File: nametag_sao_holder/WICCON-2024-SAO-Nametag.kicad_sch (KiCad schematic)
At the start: 25 parts, among them J1 SAO, J2 SAO, J3 SAO, J4 SAO, J5 SAO, J6 SAO, J7 SAO, J8 SAO, SW1 ON/OFF, U1 QX2303L33E

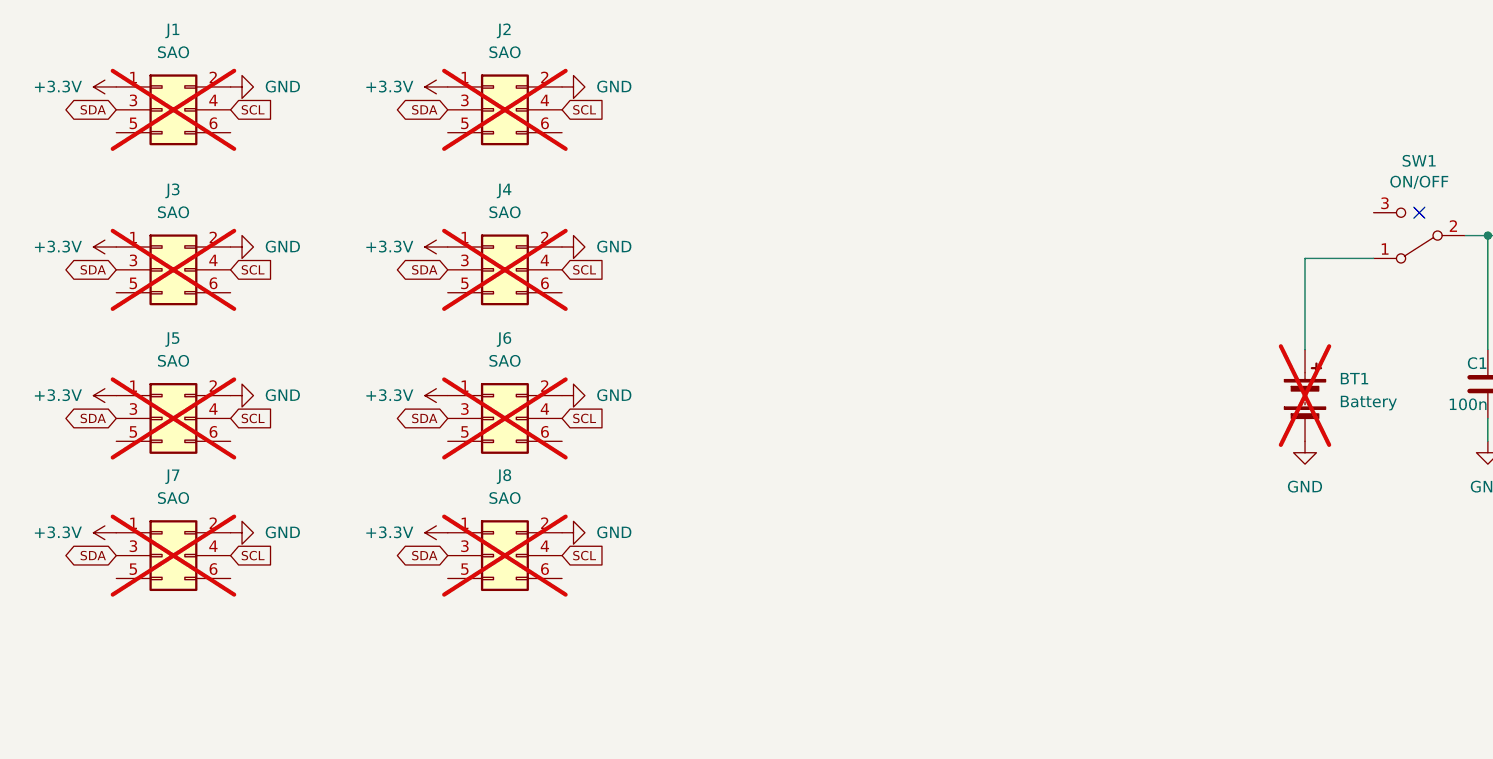
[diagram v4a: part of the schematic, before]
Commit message: Add SAO connector LCSC number, place all SAO connectors & battery holder
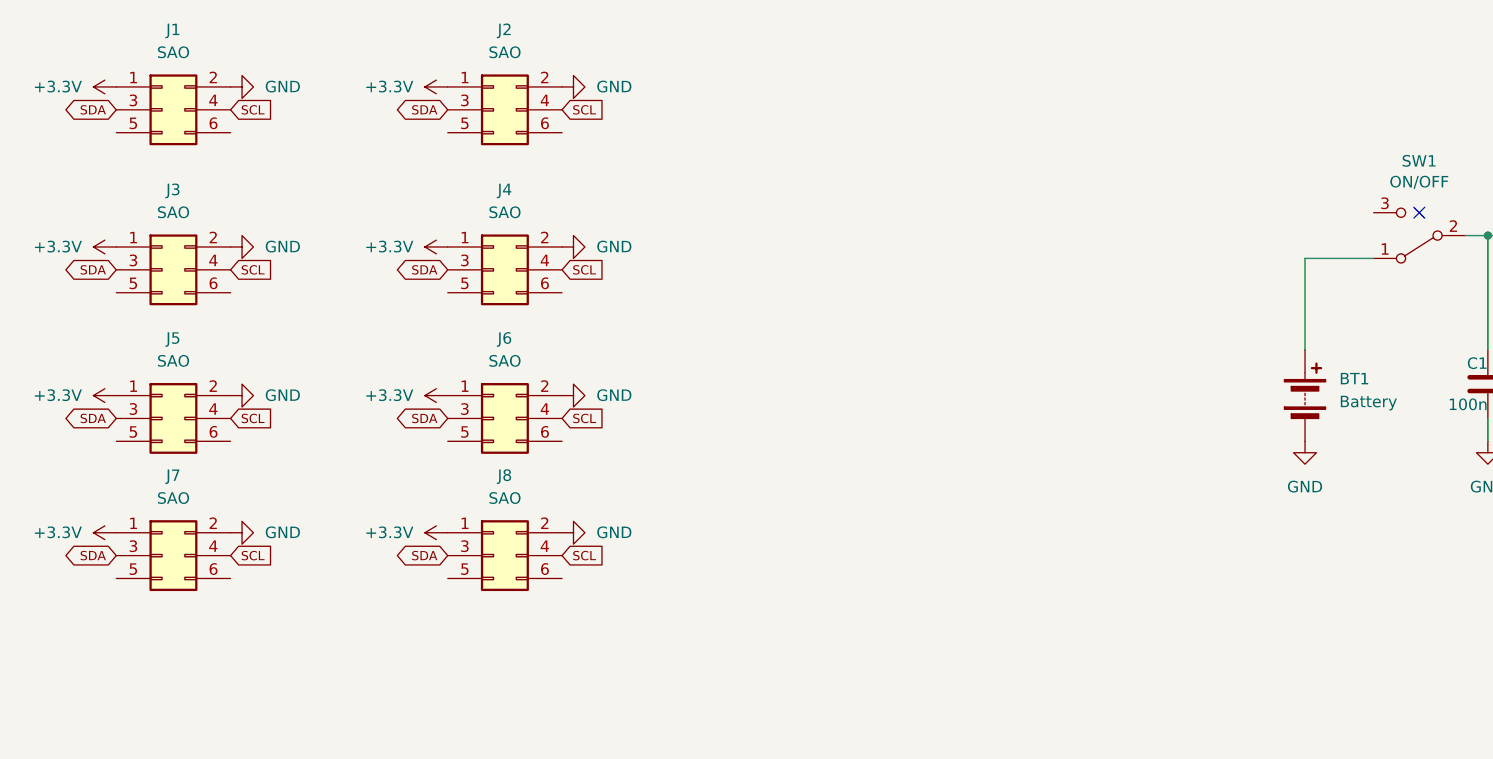
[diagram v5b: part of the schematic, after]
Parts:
- BT1: now fitted; now in the parts list
- J1, J2, J3, J4, J5, J6, J7, J8: LCSC (none) -> C92272; now fitted; now in the parts list
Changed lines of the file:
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@@
 			)
 		)
-		(property "Description" "Housing"
+		(property "Description" ""
 			(at 265.43 132.08 0)
 			(effects
@@
 			)
 		)
-		(property "Description" "Housing"
+		(property "Description" ""
 			(at 265.43 144.78 0)
 			(effects
@@
 			)
 		)
-		(property "Description" "RED LED"
+		(property "Description" "Red LED"
 			(at 250.19 50.8 0)
 			(effects
@@
 			)
 		)
-		(property "Description" "Mounting Hole without connection"
+		(property "Description" ""
 			(at 250.19 158.75 0)
 			(effects
@@
 			)
 		)
-		(property "Description" "Mounting Hole without connection"
+		(property "Description" ""
 			(at 250.19 153.67 0)
 			(effects
@@
 			)
 		)
-		(property "Description" "Housing"
+		(property "Description" ""
 			(at 265.43 120.65 0)
 			(effects
@@
 		(unit 1)
 		(exclude_from_sim no)
-		(in_bom no)
+		(in_bom yes)
 		(on_board yes)
-		(dnp yes)
+		(dnp no)
 		(fields_autoplaced yes)
 		(property "Reference" "J3"
@@
 			)
 		)
-		(property "Description" "Generic connector, double row, 02x03, odd/even pin numbering scheme (row 1 odd numbers, row 2 even numbers), script generated (kicad-library-utils/schlib/autogen/connector/)"
+		(property "Description" ""
+			(at 45.72 48.26 0)
+			(effects
+				(font
+					(size 1.27 1.27)
+				)
+				(hide yes)
+			)
+		)
+		(property "LCSC" "C92272"
 			(at 45.72 48.26 0)
 			(effects
@@
 		(unit 1)
 		(exclude_from_sim no)
-		(in_bom no)
+		(in_bom yes)
 		(on_board yes)
-		(dnp yes)
+		(dnp no)
 		(fields_autoplaced yes)
 		(property "Reference" "J7"
@@
 			)
 		)
-		(property "Description" "Generic connector, double row, 02x03, odd/even pin numbering scheme (row 1 odd numbers, row 2 even numbers), script generated (kicad-library-utils/schlib/autogen/connector/)"
+		(property "Description" ""
+			(at 45.72 80.01 0)
+			(effects
+				(font
+					(size 1.27 1.27)
+				)
+				(hide yes)
+			)
+		)
+		(property "LCSC" "C92272"
 			(at 45.72 80.01 0)
 			(effects
@@
 		(unit 1)
 		(exclude_from_sim no)
-		(in_bom no)
+		(in_bom yes)
 		(on_board yes)
-		(dnp yes)
+		(dnp no)
 		(fields_autoplaced yes)
 		(property "Reference" "J1"
@@
 			)
 		)
-		(property "Description" "Generic connector, double row, 02x03, odd/even pin numbering scheme (row 1 odd numbers, row 2 even numbers), script generated (kicad-library-utils/schlib/autogen/connector/)"
+		(property "Description" ""
+			(at 45.72 30.48 0)
+			(effects
+				(font
+					(size 1.27 1.27)
+				)
+				(hide yes)
+			)
+		)
+		(property "LCSC" "C92272"
 			(at 45.72 30.48 0)
 			(effects
@@
 		(unit 1)
 		(exclude_from_sim no)
-		(in_bom no)
+		(in_bom yes)
 		(on_board yes)
-		(dnp yes)
+		(dnp no)
 		(fields_autoplaced yes)
 		(property "Reference" "J5"
@@
 			)
 		)
-		(property "Description" "Generic connector, double row, 02x03, odd/even pin numbering scheme (row 1 odd numbers, row 2 even numbers), script generated (kicad-library-utils/schlib/autogen/connector/)"
+		(property "Description" ""
+			(at 45.72 64.77 0)
+			(effects
+				(font
+					(size 1.27 1.27)
+				)
+				(hide yes)
+			)
+		)
+		(property "LCSC" "C92272"
 			(at 45.72 64.77 0)
 			(effects
@@
 		(unit 1)
 		(exclude_from_sim no)
-		(in_bom no)
+		(in_bom yes)
 		(on_board yes)
-		(dnp yes)
+		(dnp no)
 		(fields_autoplaced yes)
 		(property "Reference" "J8"
@@
 			)
 		)
-		(property "Description" "Generic connector, double row, 02x03, odd/even pin numbering scheme (row 1 odd numbers, row 2 even numbers), script generated (kicad-library-utils/schlib/autogen/connector/)"
+		(property "Description" ""
+			(at 82.55 80.01 0)
+			(effects
+				(font
+					(size 1.27 1.27)
+				)
+				(hide yes)
+			)
+		)
+		(property "LCSC" "C92272"
 			(at 82.55 80.01 0)
 			(effects
@@
 			)
 		)
-		(property "Description" "Housing"
+		(property "Description" ""
 			(at 265.43 154.94 0)
 			(effects
@@
 		(unit 1)
 		(exclude_from_sim no)
-		(in_bom no)
+		(in_bom yes)
 		(on_board yes)
-		(dnp yes)
+		(dnp no)
 		(fields_autoplaced yes)
 		(property "Reference" "J4"
@@
 			)
 		)
-		(property "Description" "Generic connector, double row, 02x03, odd/even pin numbering scheme (row 1 odd numbers, row 2 even numbers), script generated (kicad-library-utils/schlib/autogen/connector/)"
+		(property "Description" ""
+			(at 82.55 48.26 0)
+			(effects
+				(font
+					(size 1.27 1.27)
+				)
+				(hide yes)
+			)
+		)
+		(property "LCSC" "C92272"
 			(at 82.55 48.26 0)
 			(effects
@@
 		(unit 1)
 		(exclude_from_sim no)
-		(in_bom no)
+		(in_bom yes)
 		(on_board yes)
-		(dnp yes)
+		(dnp no)
 		(fields_autoplaced yes)
 		(property "Reference" "J2"
@@
 			)
 		)
-		(property "Description" "Generic connector, double row, 02x03, odd/even pin numbering scheme (row 1 odd numbers, row 2 even numbers), script generated (kicad-library-utils/schlib/autogen/connector/)"
+		(property "Description" ""
+			(at 82.55 30.48 0)
+			(effects
+				(font
+					(size 1.27 1.27)
+				)
+				(hide yes)
+			)
+		)
+		(property "LCSC" "C92272"
 			(at 82.55 30.48 0)
 			(effects
@@
 		(unit 1)
 		(exclude_from_sim no)
-		(in_bom no)
+		(in_bom yes)
 		(on_board yes)
-		(dnp yes)
+		(dnp no)
 		(fields_autoplaced yes)
 		(property "Reference" "BT1"
@@
 			)
 		)
-		(property "Description" "Multiple-cell battery"
+		(property "Description" "2x AAA"
 			(at 172.72 62.23 0)
 			(effects
@@
 		(unit 1)
 		(exclude_from_sim no)
-		(in_bom no)
+		(in_bom yes)
 		(on_board yes)
-		(dnp yes)
+		(dnp no)
 		(fields_autoplaced yes)
 		(property "Reference" "J6"
@@
 			)
 		)
-		(property "Description" "Generic connector, double row, 02x03, odd/even pin numbering scheme (row 1 odd numbers, row 2 even numbers), script generated (kicad-library-utils/schlib/autogen/connector/)"
+		(property "Description" ""
+			(at 82.55 64.77 0)
+			(effects
+				(font
+					(size 1.27 1.27)
+				)
+				(hide yes)
+			)
+		)
+		(property "LCSC" "C92272"
 			(at 82.55 64.77 0)
 			(effects

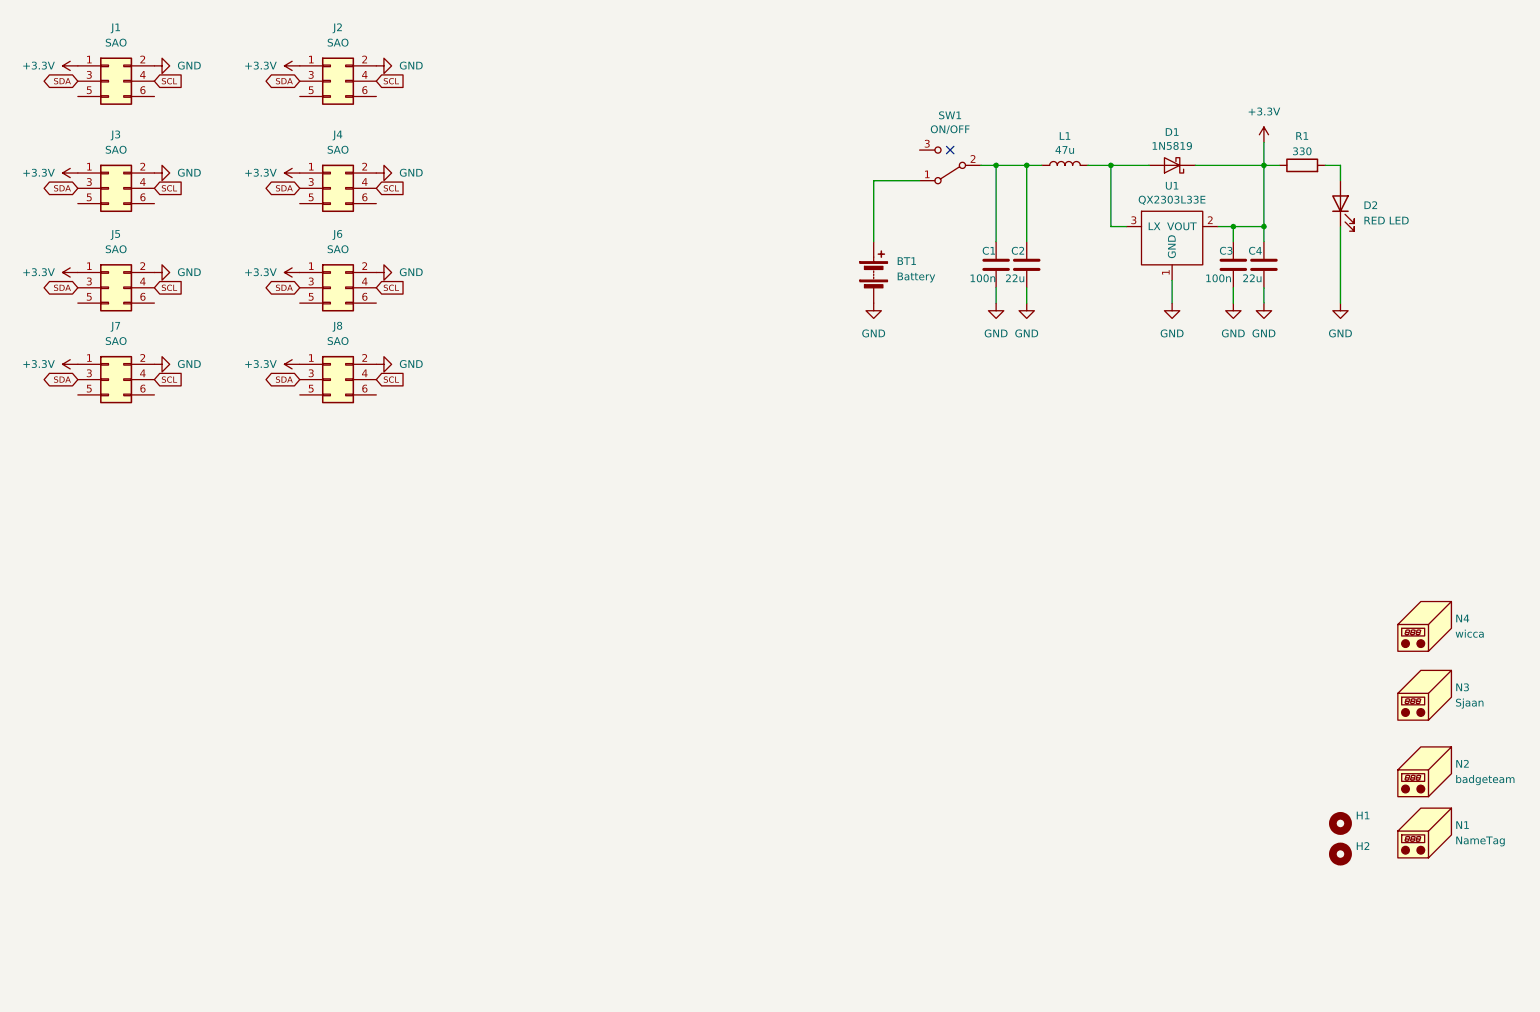
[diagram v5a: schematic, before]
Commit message: Fix I2C troubles, add connectors
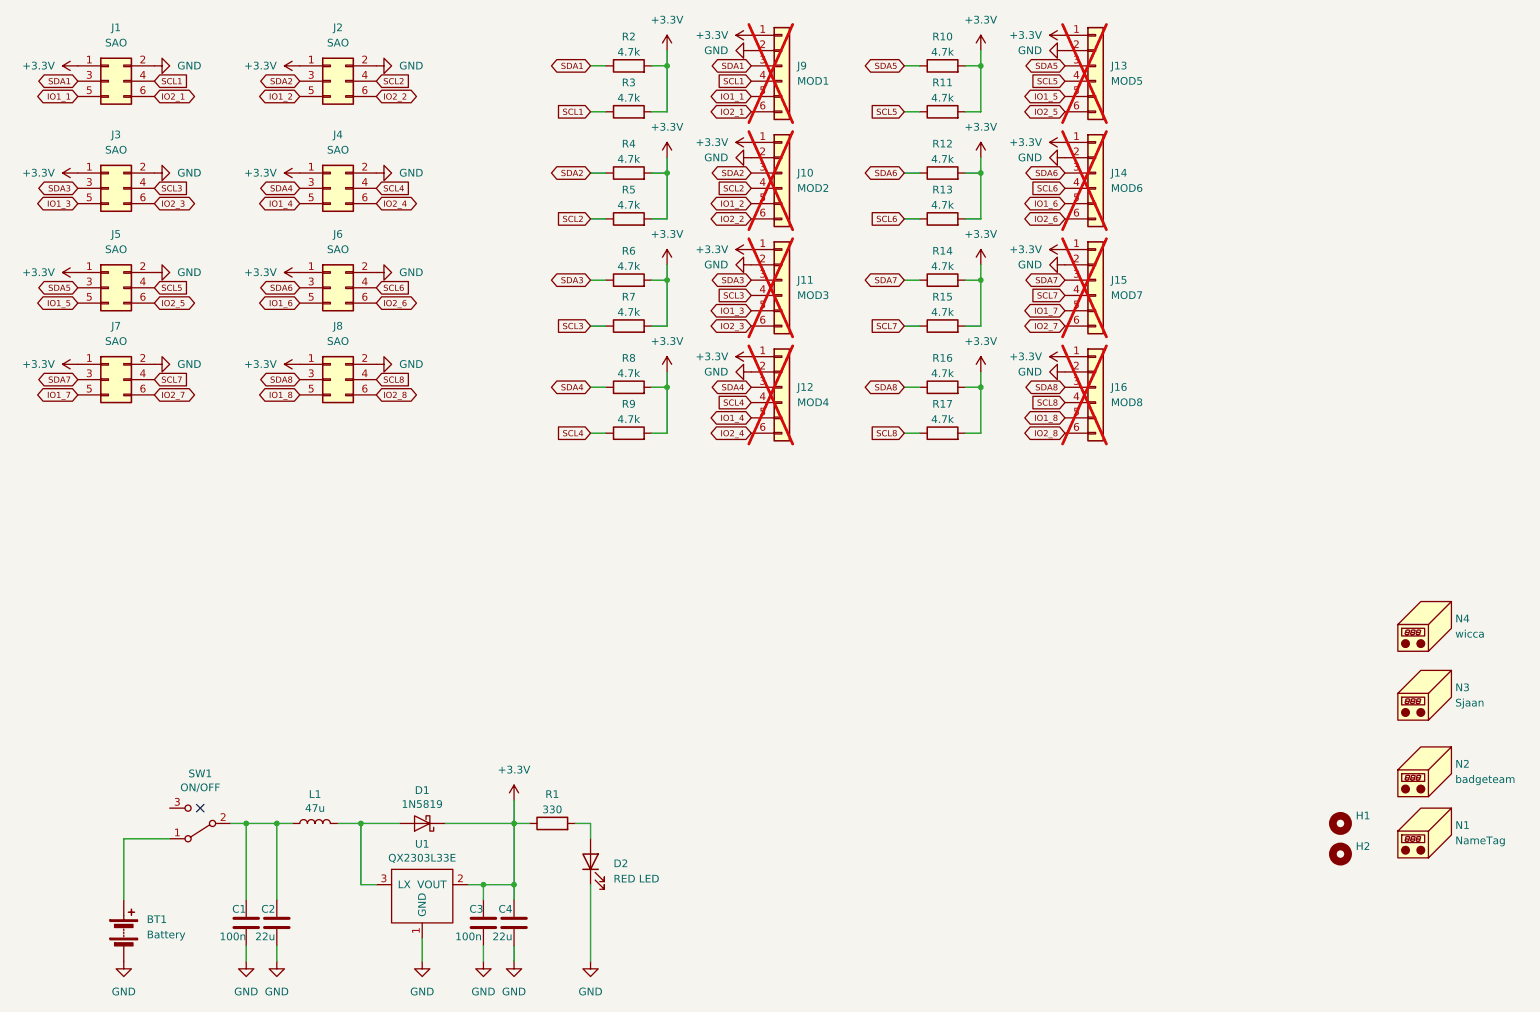
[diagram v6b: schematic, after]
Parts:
- added J10: MOD2, Connector_PinHeader_2.54mm:PinHeader_1x06_P2.54mm_Vertical_SMD_Pin1Left, symbol Connector_Generic:Conn_01x06
- added J11: MOD3, Connector_PinHeader_2.54mm:PinHeader_1x06_P2.54mm_Vertical_SMD_Pin1Left, symbol Connector_Generic:Conn_01x06
- added J12: MOD4, Connector_PinHeader_2.54mm:PinHeader_1x06_P2.54mm_Vertical_SMD_Pin1Left, symbol Connector_Generic:Conn_01x06
- added J13: MOD5, Connector_PinHeader_2.54mm:PinHeader_1x06_P2.54mm_Vertical_SMD_Pin1Left, symbol Connector_Generic:Conn_01x06
- added J14: MOD6, Connector_PinHeader_2.54mm:PinHeader_1x06_P2.54mm_Vertical_SMD_Pin1Left, symbol Connector_Generic:Conn_01x06
- added J15: MOD7, Connector_PinHeader_2.54mm:PinHeader_1x06_P2.54mm_Vertical_SMD_Pin1Left, symbol Connector_Generic:Conn_01x06
- added J16: MOD8, Connector_PinHeader_2.54mm:PinHeader_1x06_P2.54mm_Vertical_SMD_Pin1Left, symbol Connector_Generic:Conn_01x06
- added J9: MOD1, Connector_PinHeader_2.54mm:PinHeader_1x06_P2.54mm_Vertical_SMD_Pin1Left, symbol Connector_Generic:Conn_01x06
- added R10, R11, R12, R13, R14, R15, R16, R17, R2, R3, R4, R5, R6, R7, R8, R9: 4.7k, Resistor_SMD:R_0402_1005Metric, symbol Device:R
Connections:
- net +3.3V: now also J10.1 (Pin_1), J11.1 (Pin_1), J12.1 (Pin_1), J13.1 (Pin_1), J14.1 (Pin_1), J15.1 (Pin_1), J16.1 (Pin_1), J9.1 (Pin_1), R10.2, R11.2, R12.2, R13.2, R14.2, R15.2, R16.2, R17.2, R2.2, R3.2, R4.2, R5.2, R6.2, R7.2, R8.2, R9.2
- net GND: now also J10.2 (Pin_2), J11.2 (Pin_2), J12.2 (Pin_2), J13.2 (Pin_2), J14.2 (Pin_2), J15.2 (Pin_2), J16.2 (Pin_2), J9.2 (Pin_2)
- net IO1_3: now reaches J3.5 (Pin_5)
- net IO1_3: now also J11.5 (Pin_5)
- net IO2_3: now reaches J3.6 (Pin_6)
- net IO2_3: now also J11.6 (Pin_6)
- net IO1_7: now reaches J7.5 (Pin_5)
- net IO1_7: now also J15.5 (Pin_5)
- net IO2_7: now reaches J7.6 (Pin_6)
- net IO2_7: now also J15.6 (Pin_6)
- net IO1_1: now reaches J1.5 (Pin_5)
- net IO1_1: now also J9.5 (Pin_5)
- net IO2_1: now reaches J1.6 (Pin_6)
- net IO2_1: now also J9.6 (Pin_6)
- net IO1_5: now reaches J5.5 (Pin_5)
- net IO1_5: now also J13.5 (Pin_5)
- net IO2_5: now reaches J5.6 (Pin_6)
- net IO2_5: now also J13.6 (Pin_6)
- net IO1_8: now reaches J8.5 (Pin_5)
- net IO1_8: now also J16.5 (Pin_5)
- net IO2_8: now reaches J8.6 (Pin_6)
- net IO2_8: now also J16.6 (Pin_6)
- net IO1_4: now reaches J4.5 (Pin_5)
- net IO1_4: now also J12.5 (Pin_5)
- net IO2_4: now reaches J4.6 (Pin_6)
- net IO2_4: now also J12.6 (Pin_6)
- net IO1_2: now reaches J2.5 (Pin_5)
- net IO1_2: now also J10.5 (Pin_5)
- net IO2_2: now reaches J2.6 (Pin_6)
- net IO2_2: now also J10.6 (Pin_6)
- net IO1_6: now reaches J6.5 (Pin_5)
- net IO1_6: now also J14.5 (Pin_5)
- net IO2_6: now reaches J6.6 (Pin_6)
- net IO2_6: now also J14.6 (Pin_6)
- removed net SCL: J1.4 (Pin_4), J2.4 (Pin_4), J3.4 (Pin_4), J4.4 (Pin_4), J5.4 (Pin_4), J6.4 (Pin_4), J7.4 (Pin_4), J8.4 (Pin_4)
- removed net SDA: J1.3 (Pin_3), J2.3 (Pin_3), J3.3 (Pin_3), J4.3 (Pin_3), J5.3 (Pin_3), J6.3 (Pin_3), J7.3 (Pin_3), J8.3 (Pin_3)
- new net SCL1: J1.4 (Pin_4), J9.4 (Pin_4), R3.1
- new net SCL2: J10.4 (Pin_4), J2.4 (Pin_4), R5.1
- new net SCL3: J11.4 (Pin_4), J3.4 (Pin_4), R7.1
- new net SCL4: J12.4 (Pin_4), J4.4 (Pin_4), R9.1
- new net SCL5: J13.4 (Pin_4), J5.4 (Pin_4), R11.1
- new net SCL6: J14.4 (Pin_4), J6.4 (Pin_4), R13.1
- new net SCL7: J15.4 (Pin_4), J7.4 (Pin_4), R15.1
- new net SCL8: J16.4 (Pin_4), J8.4 (Pin_4), R17.1
- new net SDA1: J1.3 (Pin_3), J9.3 (Pin_3), R2.1
- new net SDA2: J10.3 (Pin_3), J2.3 (Pin_3), R4.1
- new net SDA3: J11.3 (Pin_3), J3.3 (Pin_3), R6.1
- new net SDA4: J12.3 (Pin_3), J4.3 (Pin_3), R8.1
- new net SDA5: J13.3 (Pin_3), J5.3 (Pin_3), R10.1
- new net SDA6: J14.3 (Pin_3), J6.3 (Pin_3), R12.1
- new net SDA7: J15.3 (Pin_3), J7.3 (Pin_3), R14.1
- new net SDA8: J16.3 (Pin_3), J8.3 (Pin_3), R16.1
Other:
- moved on the sheet: BT1, C1, C2, C3, C4, D1, D2, L1, R1, SW1, U1

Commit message: Add 100k pull-up to SDA on social battery and use correct footprint for battery holder on SAO nametag
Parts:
- BT1: footprint Library:BatteryHolder_Keystone_2468_2xAAA_noholes -> Library:BAT-TH_BH-BH-AAA-A1AJ020
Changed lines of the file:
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@@
 			)
 		)
-		(property "Footprint" "Library:BatteryHolder_Keystone_2468_2xAAA_noholes"
+		(property "Footprint" "Library:BAT-TH_BH-BH-AAA-A1AJ020"
 			(at 48.26 169.926 90)
 			(effects
